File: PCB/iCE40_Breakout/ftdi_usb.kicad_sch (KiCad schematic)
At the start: 57 parts, among them J2 Conn_01x08, J4 USB_C_Receptacle_USB2.0_16P, Q2 L2N7002SLLT1G, Q3 L2N7002SLLT1G, Q4 L2N7002SLLT1G, Q5 L2N7002SLLT1G, U7 FT2232HPQ, U8 93LC66BT-I/SN, Y1 X3S012000FK1H-HV

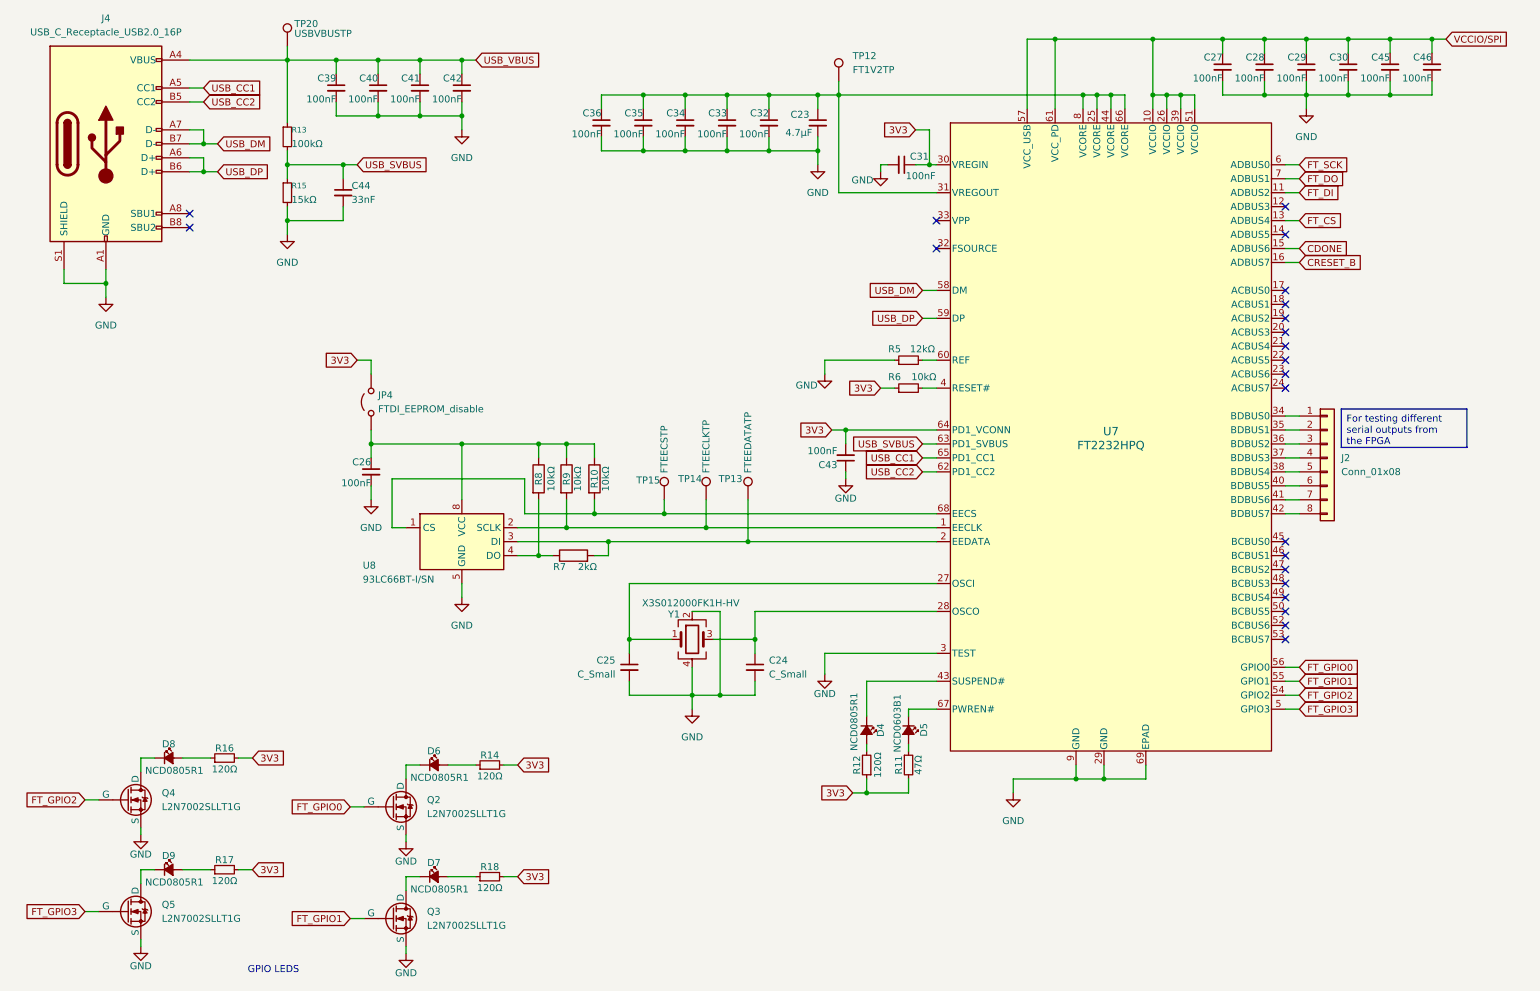
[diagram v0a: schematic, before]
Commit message: Added sheet information, and fixed ERC errors
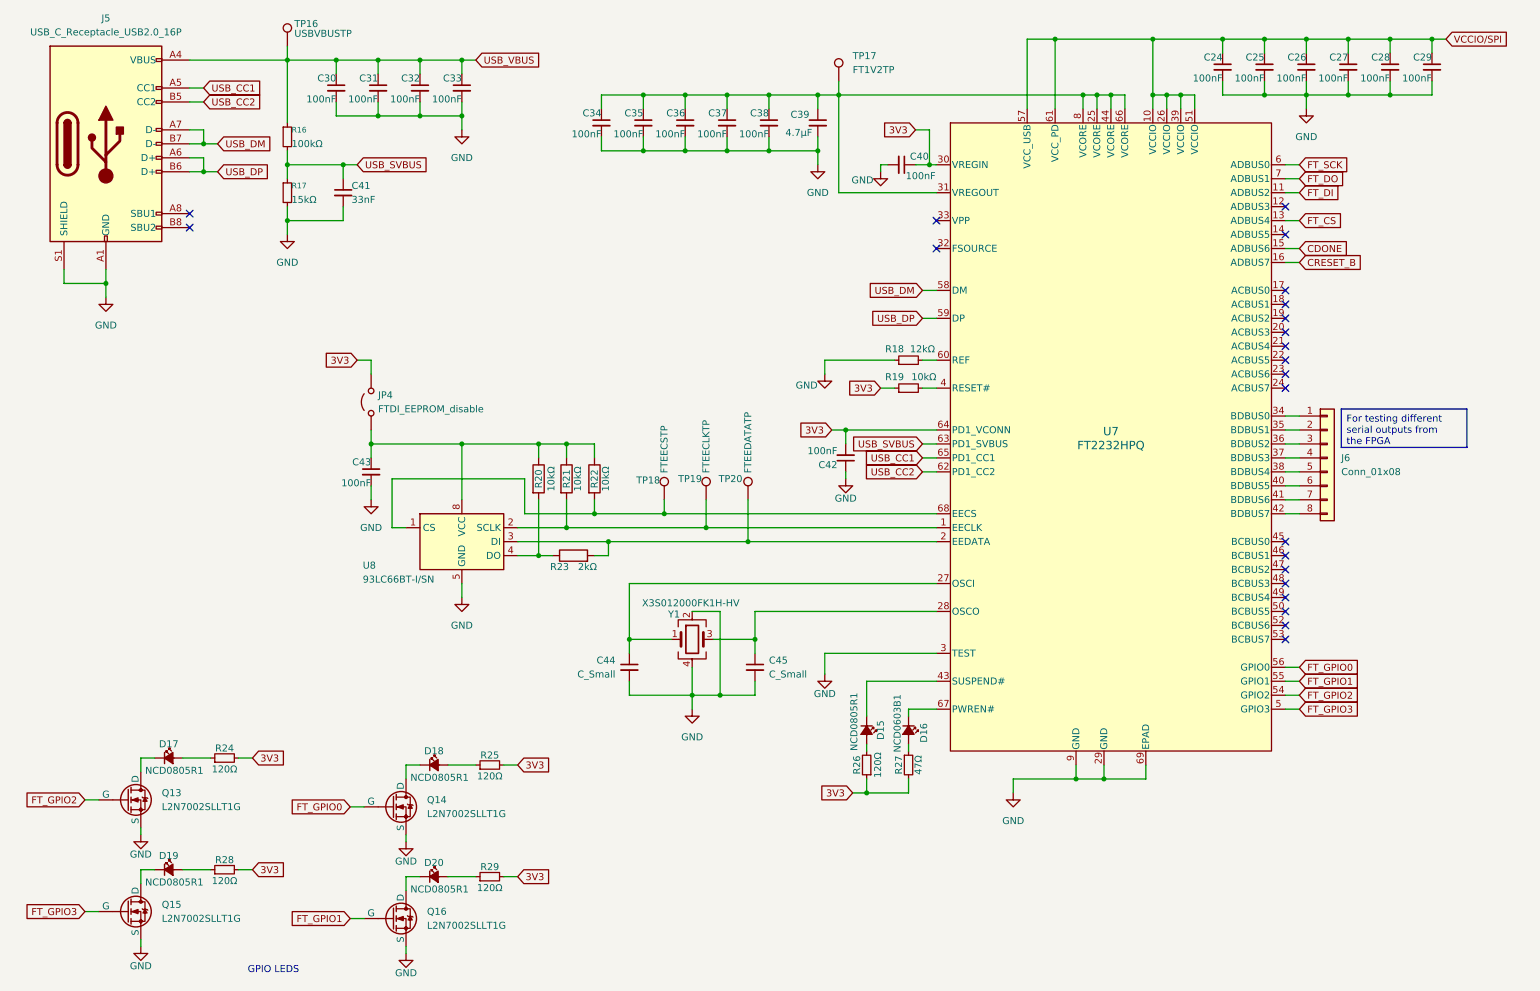
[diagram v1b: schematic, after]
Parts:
- renumbered C27 to C24, C28 to C25, C29 to C26, C30 to C27, C45 to C28, C46 to C29, C39 to C30, C40 to C31, C41 to C32, C42 to C33, C36 to C34, C34 to C36, C33 to C37, C32 to C38, C23 to C39, C31 to C40, C44 to C41, C43 to C42, C26 to C43, C25 to C44, C24 to C45, D4 to D15, D5 to D16, D8 to D17, D6 to D18, D9 to D19, D7 to D20, J4 to J5, J2 to J6, Q4 to Q13, Q2 to Q14, Q5 to Q15, Q3 to Q16, R13 to R16, R15 to R17, R5 to R18, R6 to R19, R8 to R20, R9 to R21, R10 to R22, R7 to R23, R16 to R24, R14 to R25, R12 to R26, R11 to R27, R17 to R28, R18 to R29, TP20 to TP16, TP12 to TP17, TP15 to TP18, TP14 to TP19, TP13 to TP20
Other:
- company: (none) -> S3I
- title: (none) -> iCE40 Breakout

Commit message: Added missing footprints
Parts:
- C44, C45: footprint (none) -> Capacitor_SMD:C_0402_1005Metric
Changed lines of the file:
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@@
 			)
 		)
-		(property "Footprint" ""
+		(property "Footprint" "Capacitor_SMD:C_0402_1005Metric"
 			(at 146.05 135.89 0)
 			(effects
@@
 	)
 	(symbol
+		(lib_id "power:PWR_FLAG")
+		(at 76.2 95.25 90)
+		(unit 1)
+		(exclude_from_sim no)
+		(in_bom yes)
+		(on_board yes)
+		(dnp no)
+		(fields_autoplaced yes)
+		(property "Reference" "#FLG03"
+			(at 74.295 95.25 0)
+			(effects
+				(font
+					(size 1.27 1.27)
+				)
+				(hide yes)
+			)
+		)
+		(property "Value" "PWR_FLAG"
+			(at 72.39 95.2499 90)
+			(effects
+				(font
+					(size 1.27 1.27)
+				)
+				(justify left)
+			)
+		)
+		(property "Footprint" ""
+			(at 76.2 95.25 0)
+			(effects
+				(font
+					(size 1.27 1.27)
+				)
+				(hide yes)
+			)
+		)
+		(property "Datasheet" "~"
+			(at 76.2 95.25 0)
+			(effects
+				(font
+					(size 1.27 1.27)
+				)
+				(hide yes)
+			)
+		)
+		(property "Description" "Special symbol for telling ERC where power comes from"
+			(at 76.2 95.25 0)
+			(effects
+				(font
+					(size 1.27 1.27)
+				)
+				(hide yes)
+			)
+		)
+		(pin "1"
+		)
+		(instances
+			(project "iCE40_Breakout"
+				(path "/ce4d7974-ef38-4eea-8119-381c4298ef02/a0447fef-6cc5-400b-aa41-8540b8ebce1f"
+					(reference "#FLG03")
+					(unit 1)
+				)
+			)
+		)
+	)
+	(symbol
 		(lib_id "power:GND")
 		(at 92.71 123.19 0)
@@
 			)
 		)
-		(property "Footprint" ""
+		(property "Footprint" "Capacitor_SMD:C_0402_1005Metric"
 			(at 123.19 135.89 0)
 			(effects

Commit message: Changed LED footprints to be from LED lib, and not the Diode lib
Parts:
- D15, D17, D18, D19, D20: footprint Diode_SMD:D_0805_2012Metric -> LED_SMD:LED_0805_2012Metric
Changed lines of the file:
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@@
 			)
 		)
-		(property "Footprint" "Diode_SMD:D_0805_2012Metric"
+		(property "Footprint" "LED_SMD:LED_0805_2012Metric"
 			(at 39.37 172.72 90)
 			(effects
@@
 			)
 		)
-		(property "Footprint" "Diode_SMD:D_0805_2012Metric"
+		(property "Footprint" "LED_SMD:LED_0805_2012Metric"
 			(at 87.63 173.99 90)
 			(effects
@@
 			)
 		)
-		(property "Footprint" "Diode_SMD:D_0805_2012Metric"
+		(property "Footprint" "LED_SMD:LED_0805_2012Metric"
 			(at 87.63 153.67 90)
 			(effects
@@
 			)
 		)
-		(property "Footprint" "Diode_SMD:D_0805_2012Metric"
+		(property "Footprint" "LED_SMD:LED_0805_2012Metric"
 			(at 166.37 147.32 90)
 			(effects
@@
 			)
 		)
-		(property "Footprint" "Diode_SMD:D_0805_2012Metric"
+		(property "Footprint" "LED_SMD:LED_0805_2012Metric"
 			(at 39.37 152.4 90)
 			(effects

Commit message: Changed blue LED fron 0603 package to 0805 package to match other LEDs
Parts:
- D16: value NCD0603B1 -> NCD0805B2; footprint LED_SMD:LED_0603_1608Metric -> LED_SMD:LED_0805_2012Metric; LCSC C84266 -> C84259
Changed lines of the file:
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@@
 			)
 		)
-		(property "Value" "NCD0603B1"
+		(property "Value" "NCD0805B2"
 			(at 171.958 151.384 0)
 			(effects
@@
 			)
 		)
-		(property "Footprint" "LED_SMD:LED_0603_1608Metric"
+		(property "Footprint" "LED_SMD:LED_0805_2012Metric"
 			(at 173.99 147.32 90)
 			(effects
@@
 			)
 		)
-		(property "LCSC" "C84266"
+		(property "LCSC" "C84259"
 			(at 173.99 147.32 90)
 			(effects
